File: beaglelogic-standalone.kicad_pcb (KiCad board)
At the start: 4 copper layers, 100 x 60 mm, 254 parts, among them J1 USB_OTG, J2 CONN_02X02, J3 USB_A, J4 CONN_01X06, J5 SI-51009-F, J6 CONN_02X12, J7 CONN_02X16, J8 Barrel_Jack, M1 TEST_1P, M2 TEST_1P, M3 TEST_1P, M4 TEST_1P, Q1 BSS138, Q2 BSS138, SW1 SW_PUSH_SMALL_H, SW2 SW_PUSH_SMALL_H, U1 74LVC1G07, U10 MCP79410/TDFN, U11 SST26VF064B, U12 TPS73101, U13 SN74LVCH16T245, U14 DVIULC6-4SC6, U15 DVIULC6-4SC6, U16 DVIULC6-4SC6, U17 DVIULC6-4SC6, U18 74LV1T125, U19 EMMC_4G, U2 AP1117, U3 TPS2051C, U4 TPD4S012, U5 TPD4S012, U6 OSD3358-SM, U7 KSZ9031RNXCC, U8 74LVC2G241, U9 74LVC1G125, Y1 25MHz, Y2 24MHz, Y3 32.768kHz,CL=9pF

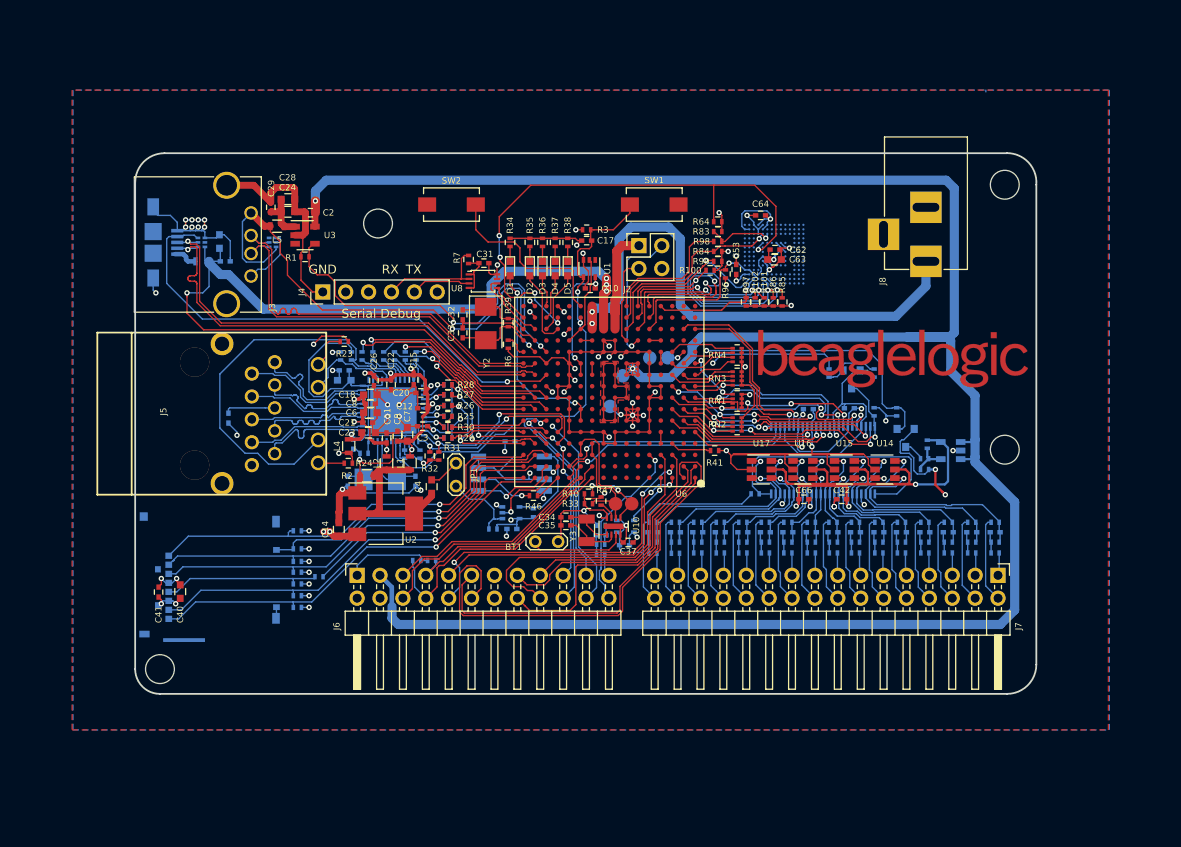
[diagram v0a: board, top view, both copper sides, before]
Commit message: Final touches to Rev A
 * Shrink logo to fit on board
 * Add fiducials on board
 * Rotate USB-A connector 90 degrees so that it does not interfere with
   microUSB
 * Add helper text

Signed-off-by: Kumar Abhishek <abhishek@theembeddedkitchen.net>
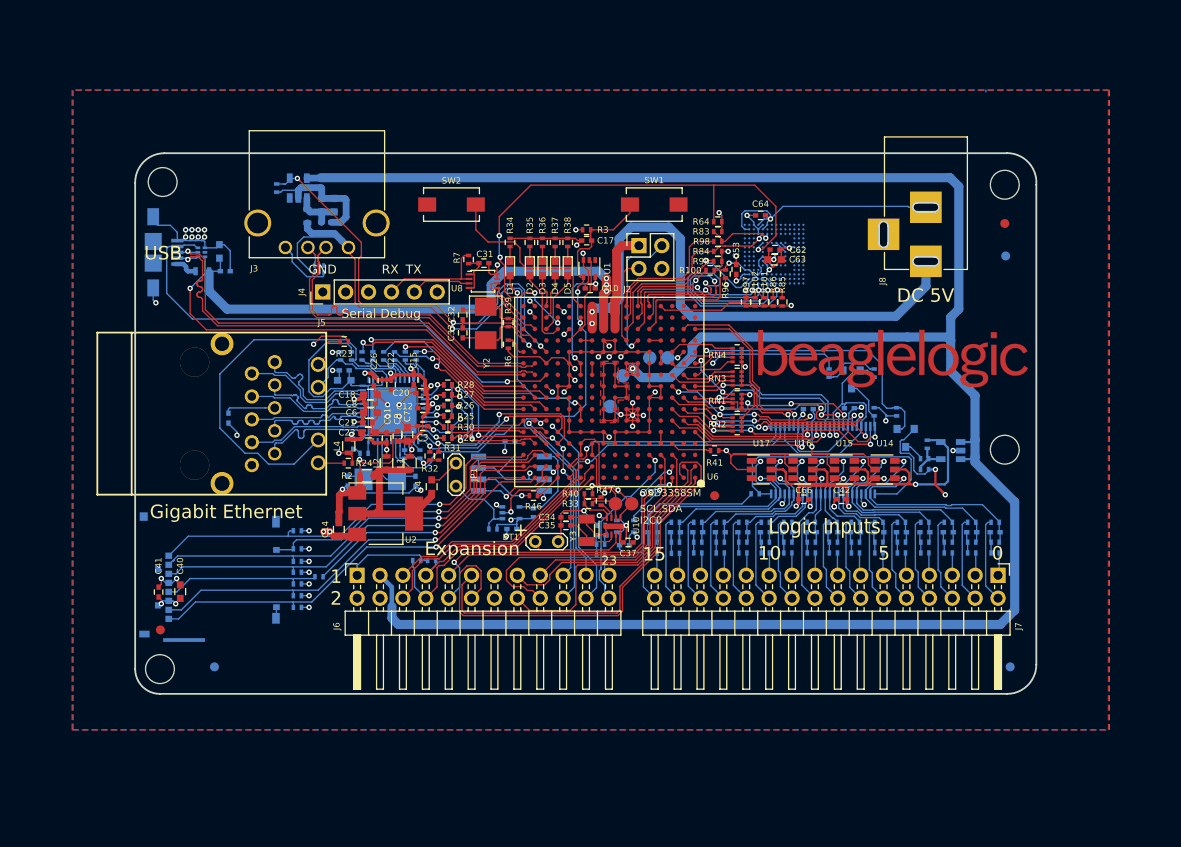
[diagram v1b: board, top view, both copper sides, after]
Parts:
- added FID1: Mounting_Hole, Fiducials:Fiducial_1mm_Dia_2.54mm_Outer_CopperTop, F.Cu at (165.3, 109.0)
- added FID2: Mounting_Hole, Fiducials:Fiducial_1mm_Dia_2.54mm_Outer_CopperTop, F.Cu at (197.5, 78.8)
- added FID3: Mounting_Hole, Fiducials:Fiducial_1mm_Dia_2.54mm_Outer_CopperTop, F.Cu at (103.8, 123.9)
- added FID4: Mounting_Hole, Fiducials:Fiducial_1mm_Dia_2.54mm_Outer_CopperTop, B.Cu at (198.1, 128.0)
- added FID5: Mounting_Hole, Fiducials:Fiducial_1mm_Dia_2.54mm_Outer_CopperTop, B.Cu at (197.6, 82.4)
- added FID6: Mounting_Hole, Fiducials:Fiducial_1mm_Dia_2.54mm_Outer_CopperTop, B.Cu at (109.8, 128.0)
- C2, C24, C28, C29, L5, R1, U3: moved to B.Cu
- D1, D2, D3, D4: value LED -> GREEN
- R104, R106, R108, R110, R112, R114, R116, R118, R66, R68, R70, R72, R74, R76, R78, R80, R82: value 1M,DNI -> 1M,S
- moved M3 24.2 mm to (104.2, 74.2)
- moved R1 8.25 mm to (116.7, 74.9), turned to 90 degrees
- moved J3 7.32 mm to (121.2, 81.5), turned to 180 degrees
- moved C29 6.38 mm to (122.2, 78.7), turned to 0 degrees
- moved U5 5.94 mm to (121.4, 83.8), turned to 0 degrees
- moved U3 5.28 mm to (119.1, 74.9), turned to 90 degrees
- moved C28 5.20 mm to (123.1, 76.8), turned to 90 degrees
- moved C24 3.82 mm to (121.7, 76.8), turned to 90 degrees
- moved L5 3.54 mm to (120.1, 78.0), turned to 90 degrees
- moved C2 3.52 mm to (121.6, 74.3), turned to 90 degrees
- moved C13 1.10 mm to (110.3, 81.9)
- moved C19 1.10 mm to (111.0, 84.1)
- moved J1 1.10 mm to (101.5, 82.0)
- moved L3 1.10 mm to (108.5, 84.1)
- moved U4 1.10 mm to (108.3, 82.0)
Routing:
- net USB1_DRVVBUS: track 41.4 -> 49.6 mm, vias 2 -> 3
- net SYS_5V: track 260.1 -> 253.2 mm, vias 2 -> 1
- net GND: track 510.6 -> 517.4 mm
- net USB1_D+: track 43.8 -> 37.8 mm
- net USB1_D-: track 43.8 -> 37.9 mm
- net USB1_VBUS: track 57.8 -> 52.0 mm
- net USB0_VBUS: track 111.2 -> 109.3 mm
- net USB0_D+: track 50.8 -> 50.1 mm
- net USB0_D-: track 50.8 -> 50.1 mm
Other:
- outline, holes or cut-outs redrawn
- board text added: "+"
- board text added: "0"
- board text added: "1 2"
- board text added: "10"
- board text added: "15"
- board text added: "23"
- board text added: "3.3V"
- board text added: "5"
- board text added: "5V"
- board text added: "BeagleLogic Standalone REV A"
- board text added: "DC 5V"
- board text added: "Expansion"
- board text added: "Gigabit Ethernet"
- board text added: "Logic Inputs"
- board text added: "OSD3358SM"
- board text added: "SCL,SDA I2C0"
- board text added: "USB"
- board text added: "WP"
- board text added: "www.beaglelogic.net"
- board text added: "© 2017 Kumar Abhishek theembeddedkitchen.net"
- board text removed: "BeagleLogic Standalone REV A Copyright © 2017 Kumar Abhishek"

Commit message: Release Candidate
 * Fix incorrect footprint for MCP79410
 * Adjust footprint for KSZ9031 adding more thermal vias in EP and modifying
   paste pattern
 * Add helper text
 * Add vias to some unused signals for testing purposes

Signed-off-by: Kumar Abhishek <abhishek@theembeddedkitchen.net>
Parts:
- J1: footprint beaglelogic-standalone:USB_MICRO_B_ST-USB-001E -> beaglelogic-standalone:10118192-0001LF
- U10: footprint Housings_DFN_QFN:DFN-8-1EP_2x3mm_Pitch0.5mm -> beaglelogic-standalone:DFN-8-1EP_3x2mm
- U7: footprint Housings_DFN_QFN:QFN-48-1EP_7x7mm_Pitch0.5mm -> beaglelogic-standalone:QFN-48-1EP_7x7mm
- moved C34 0.90 mm to (148.8, 112.3)
- moved C35 0.90 mm to (148.8, 111.4)
- moved U10 0.50 mm to (154.1, 112.9)
- moved C37 0.46 mm to (156.0, 113.8), turned to 90 degrees
- turned Y3 to 270 degrees
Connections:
- U6 pad A7: Net-(U6-PadA7) -> /VDD_ADC
- U6 pad A9: Net-(U6-PadA9) -> GND
- U6 pad B7: Net-(U6-PadB7) -> /VDD_ADC
- U6 pad B9: Net-(U6-PadB9) -> GND
- U6 pad F10: Net-(U6-PadF10) -> VDD_1V8
- U6 pad G10: Net-(U6-PadG10) -> VDD_1V8
- U6 pad H10: Net-(U6-PadH10) -> VDD_1V8
- U6 pad H11: Net-(U6-PadH11) -> VDD_1V8
- U6 pad J10: Net-(U6-PadJ10) -> VDD_1V8
- U6 pad J11: Net-(U6-PadJ11) -> VDD_1V8
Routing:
- net GND: track 517.4 -> 555.2 mm, vias 54 -> 62
- net VDD_1V8: track 1.27 -> 12.7 mm
- net /VDD_ADC: track 0.00 -> 1.27 mm
- net Net-(U6-PadF4): track 0.00 -> 0.93 mm, vias 0 -> 1
- net Net-(U6-PadB8): track 0.00 -> 0.92 mm, vias 0 -> 1
- net Net-(U6-PadG4): track 0.00 -> 0.92 mm, vias 0 -> 1
- net Net-(U6-PadA8): track 0.00 -> 0.91 mm, vias 0 -> 1
- net Net-(U6-PadB6): track 0.00 -> 0.89 mm, vias 0 -> 1
- net Net-(U6-PadC6): track 0.00 -> 0.86 mm, vias 0 -> 1
- net Net-(BT1-Pad1): track 10.9 -> 10.3 mm
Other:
- rule pad_to_mask_clearance: 0 -> 0.05
- board text added: "+3V3"
- board text added: "+5V"
- board text added: "1CS0"
- board text added: "1CS1"
- board text added: "1MISO"
- board text added: "1MOSI"
- board text added: "1SCK"
- board text added: "1_18"
- board text added: "1_19"
- board text added: "2SCL"
- board text added: "2SDA"
- board text added: "3_16"
- board text added: "3_17"
- board text added: "3_20"
- board text added: "3_21"
- board text added: "IN16"
- board text added: "PWM0A"
- board text added: "PWM0B"
- board text added: "QP0A"
- board text added: "QP0B"
- board text added: "SENSE"
- board text added: "TS"
- board text added: "U1RX"
- board text added: "U1TX"
- board text added: "VBAT"
- board text added: "VDDS_PLL"
- board text added: "VDD_CORE"

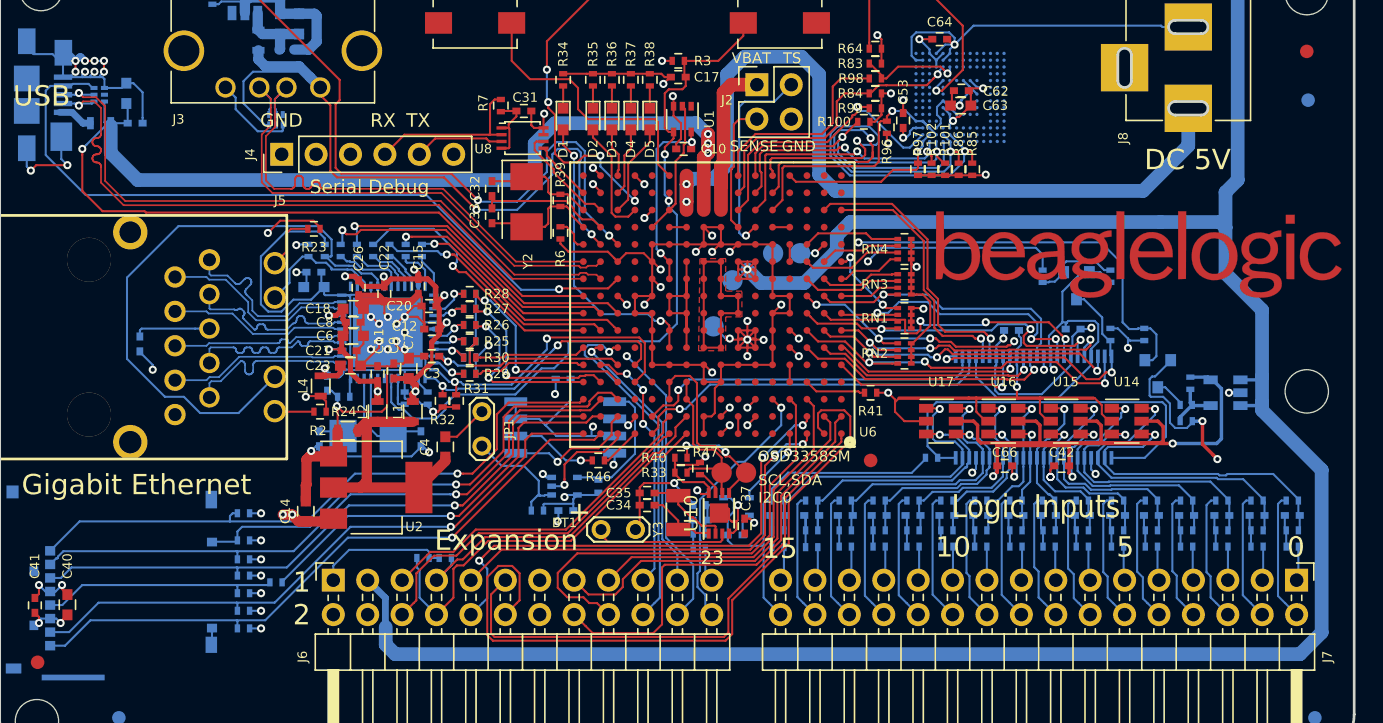
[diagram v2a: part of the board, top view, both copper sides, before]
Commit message: RC2
 * Schematic revision updated to A5
 * Add teardrops to tracks connecting to pin header pads

Signed-off-by: Kumar Abhishek <abhishek@theembeddedkitchen.net>
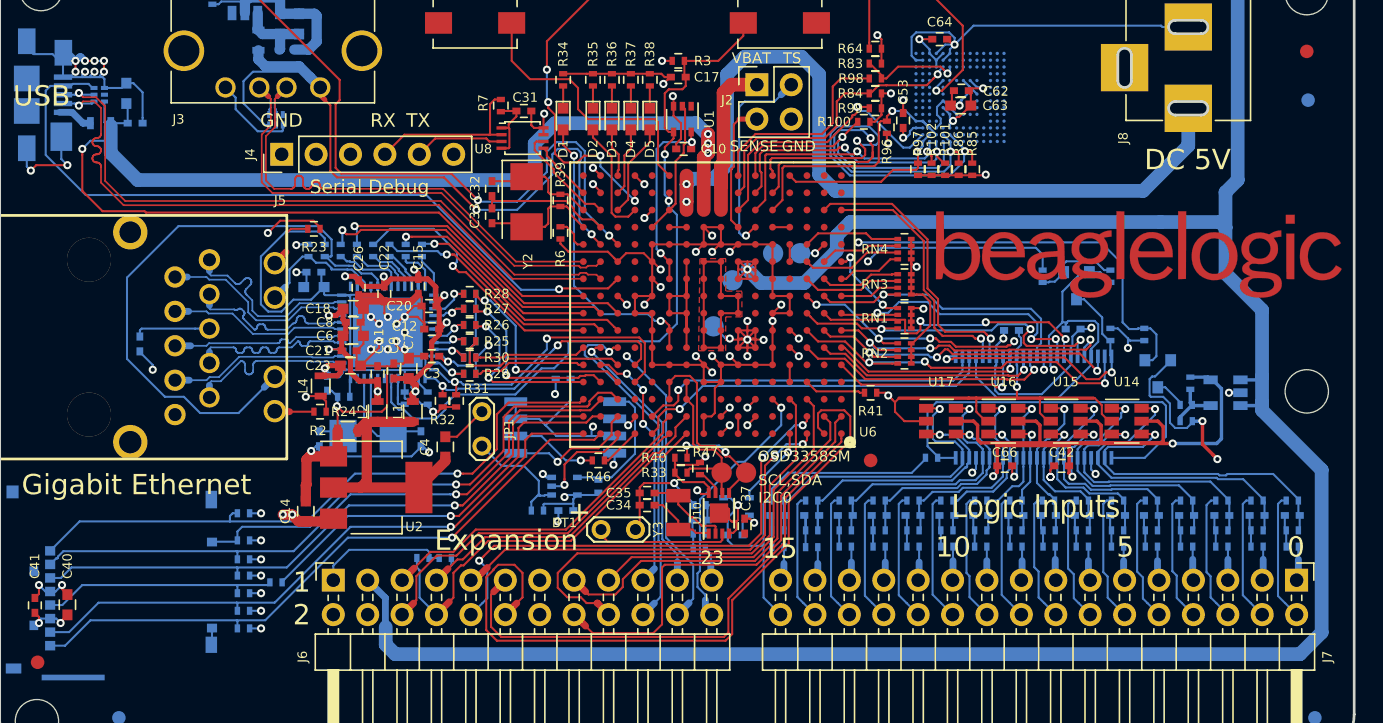
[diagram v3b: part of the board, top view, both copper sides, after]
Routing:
- net GND: track 555.2 -> 557.7 mm, vias 62 -> 66
- net /ETH_3V3: track 55.5 -> 56.8 mm
- net USB0_VBUS: track 109.4 -> 110.0 mm

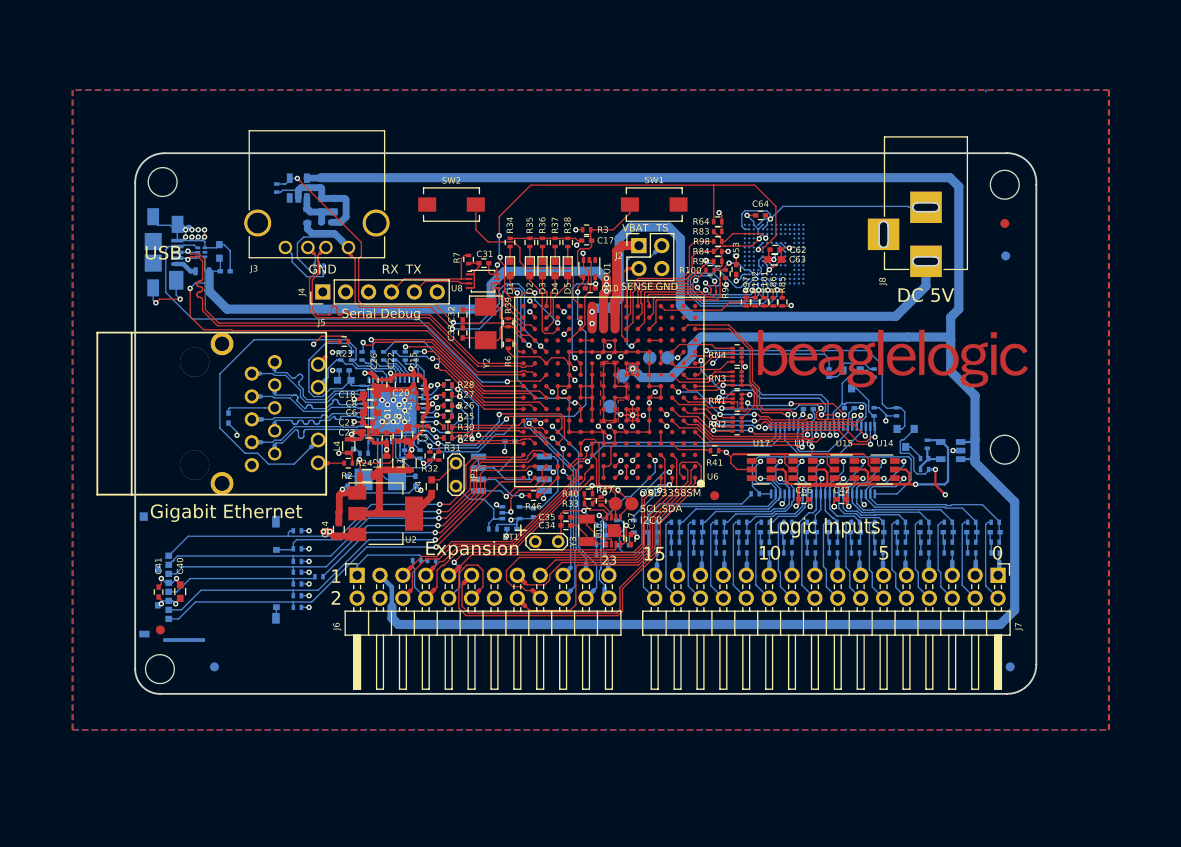
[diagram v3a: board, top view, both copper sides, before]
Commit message: Prepare design for production
 * Add breakaway rails on long edges of the PCB as required for prod
 * Remove routing from underneath the ethernet PHY QFN
 * Add triangles to indicate LED polarity on the silkscreen
 * Also add pointers on silkscreen to pin 1 of various ICs

Signed-off-by: Kumar Abhishek <abhishek@theembeddedkitchen.net>
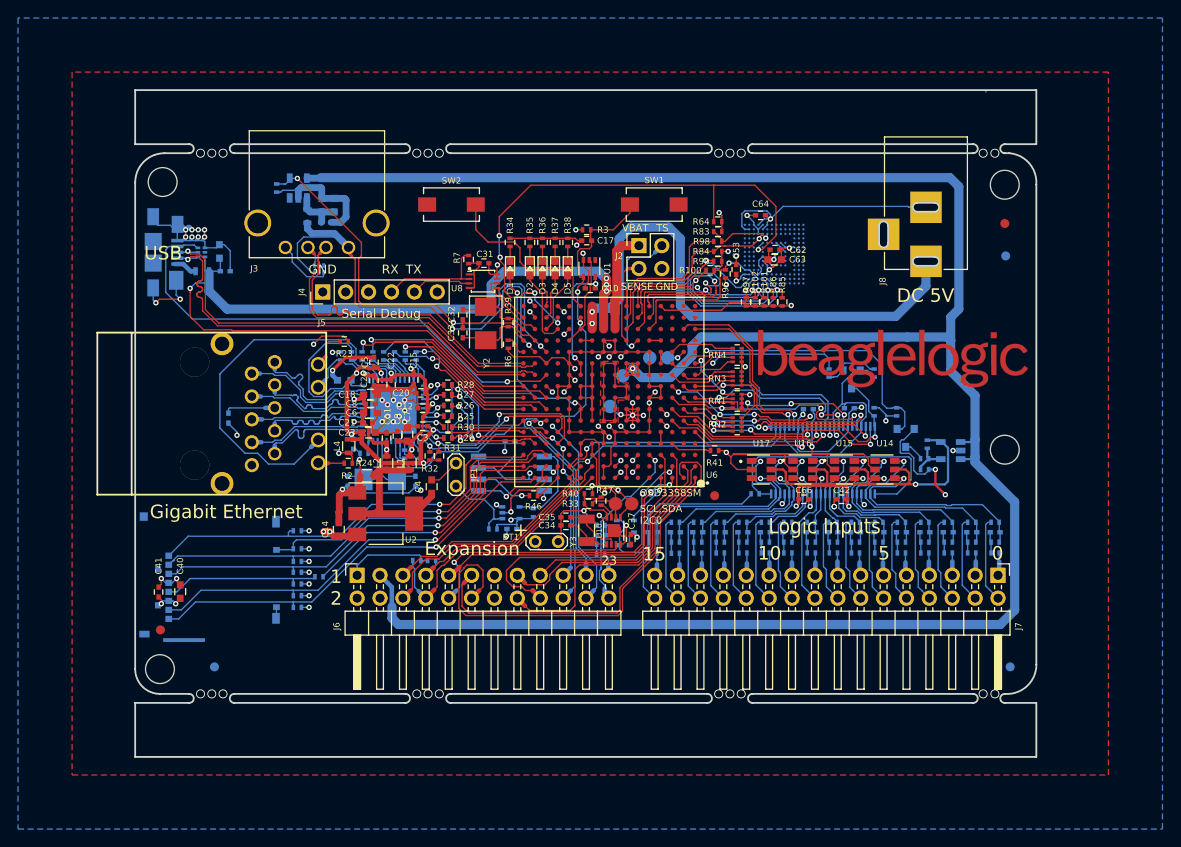
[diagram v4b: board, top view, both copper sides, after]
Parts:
- C5: moved to F.Cu
- moved C5 3.42 mm to (127.5, 94.2), turned to 90 degrees
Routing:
- net /ETH_3V3: track 56.8 -> 65.3 mm, vias 3 -> 5
- net GND: track 557.7 -> 556.6 mm
- net (no net): vias 0 -> 22
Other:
- board size 100 x 60 mm -> 100 x 74 mm
